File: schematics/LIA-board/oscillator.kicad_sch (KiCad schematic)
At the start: 7 parts, among them U6 OPA2196xD

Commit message: additions to pcb
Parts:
- added D2, D3: 1N4448W, Diode_SMD:D_SOD-123, symbol Diode:1N4448W
- added R14, R15, R16, R17, R18, R19, R20, R21, R22, R23: 1k, SparkFun-Resistor:R_0603_1608Metric, symbol SparkFun:R
- added U7: OPA2196xD, Package_SO:SOIC-8_3.9x4.9mm_P1.27mm, symbol Amplifier_Operational:OPA2196xD
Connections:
- net at C16.2, U6.7: now also R7.2, R9.1, R15.2, R18.1, R20.2; no longer R6.2
- net at C16.1, U6.6 (-): now also D2.2 (A), R17.1; no longer R9.1
- net at R9.2: now also R6.2, U6.2 (-), R14.2; no longer U6.3 (+)
- net GND: no longer names the net of C17.2
- net GND: now also R14.1, R21.2, U7.1
- new net: R17.2, R6.1, U6.1
- new net: D2.1 (K), R15.1, R16.2
- new net: R7.1, U6.3 (+)
- new net: C17.1, R20.1, U7.2 (-)
- new net: D3.1 (K), U6.5 (+), U7.3 (+)
- new net: R23.1, U7.5 (+)
- new net: R21.1, R22.2, U7.6 (-)
- new net: R22.1, U7.7
- new net: D3.2 (A), R18.2, R19.1
- now unconnected: C18.1, C18.2
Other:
- moved on the sheet: C16, C17, C18, R6, R7, R9, U6A, U6B, U6C

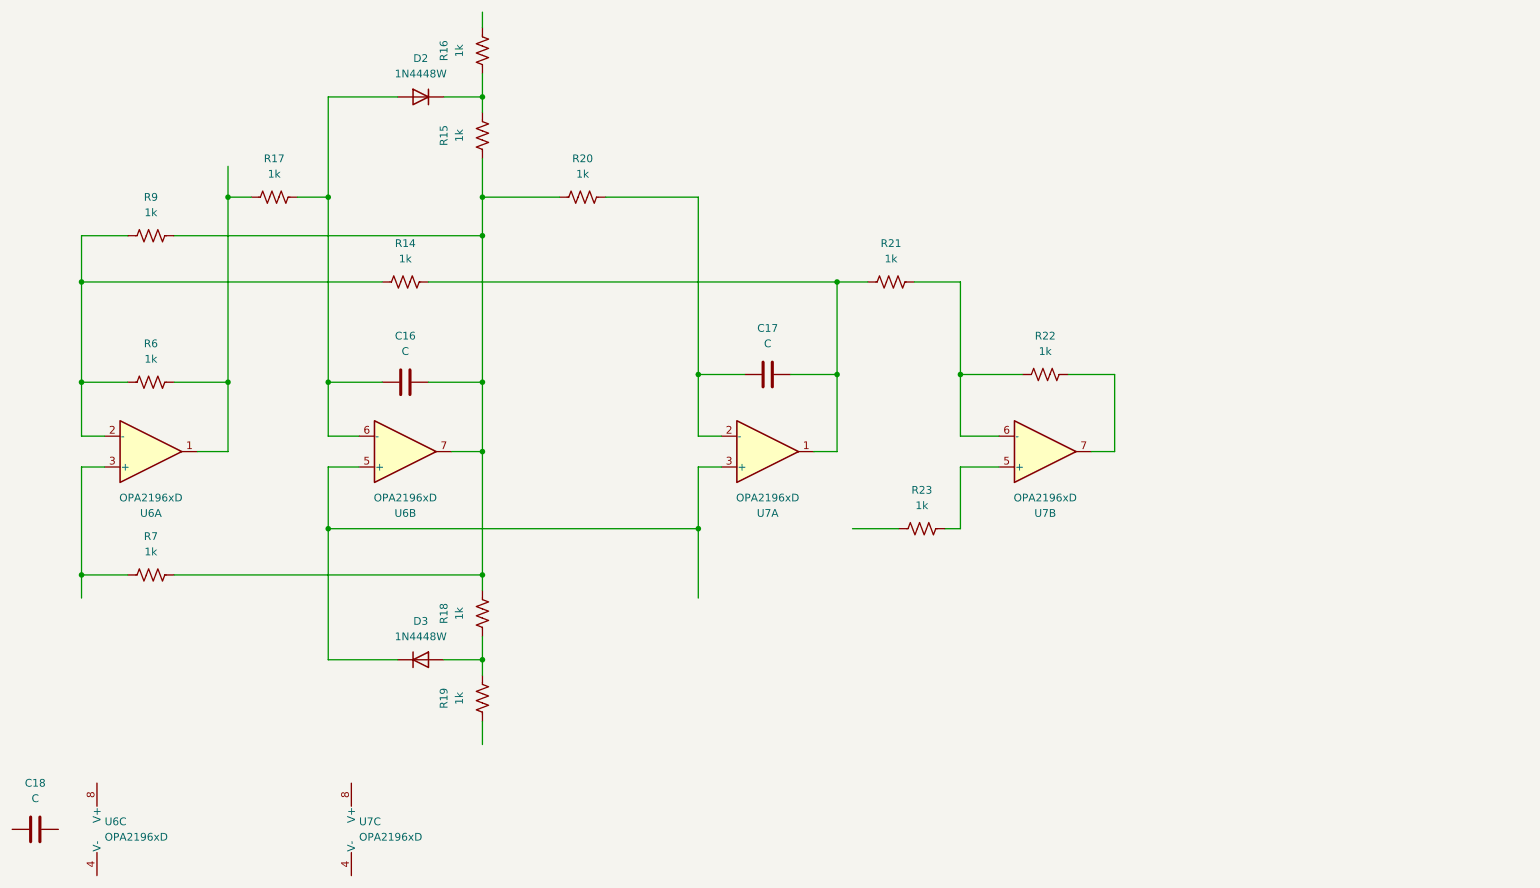
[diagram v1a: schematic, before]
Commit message: some simulations, new page in kicad scematic
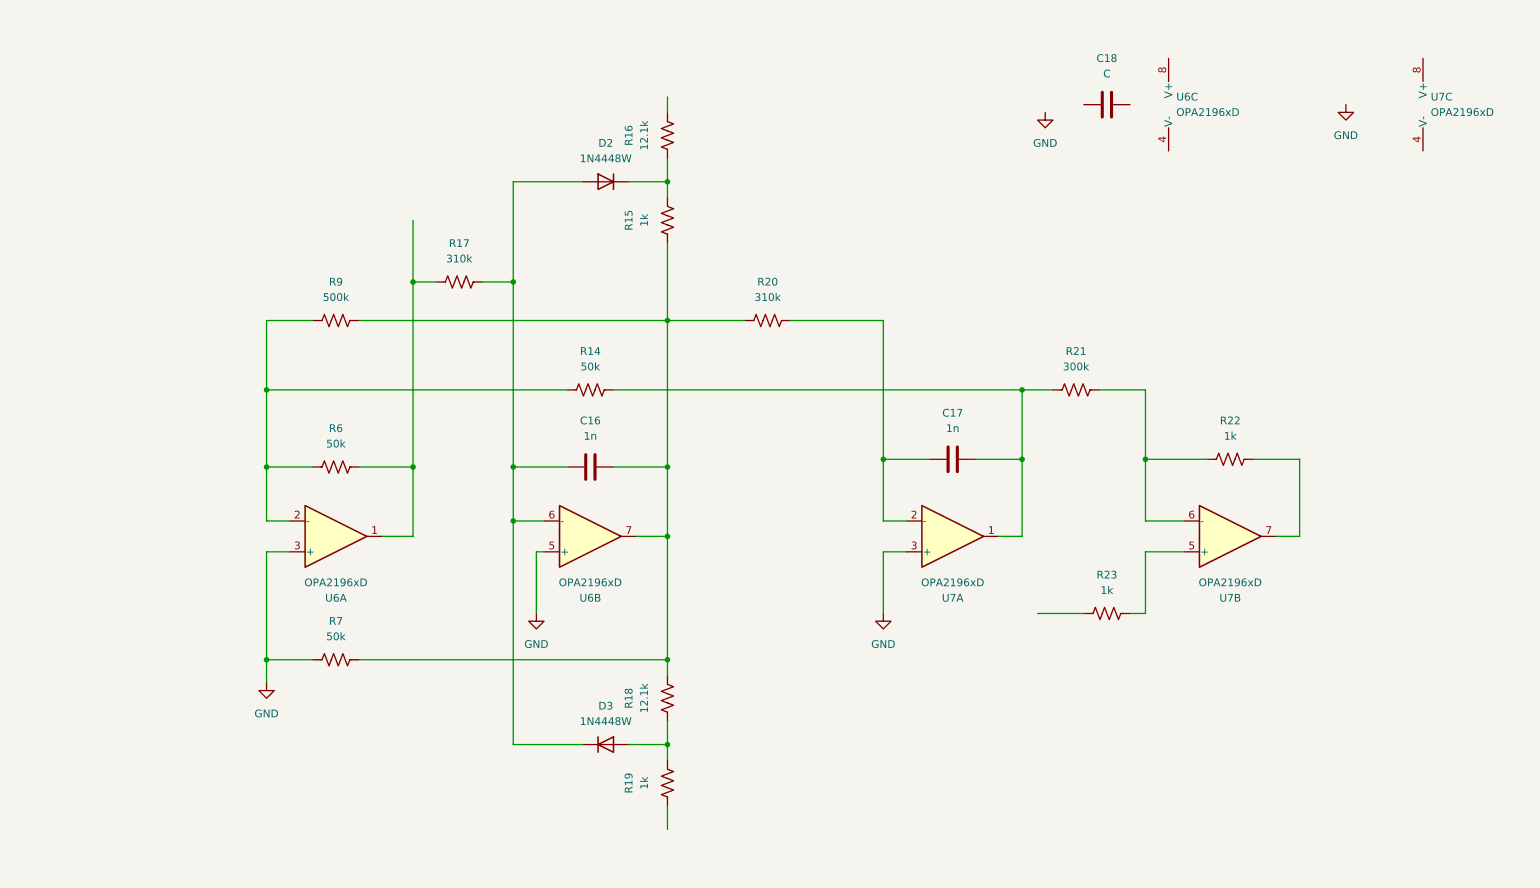
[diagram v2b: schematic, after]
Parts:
- C16, C17: value C -> 1n
- R14, R6, R7: value 1k -> 50k
- R16, R18: value 1k -> 12.1k
- R17, R20: value 1k -> 310k
- R21: value 1k -> 300k
- R9: value 1k -> 500k
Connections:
- net at C16.1, D2.2 (A), R17.1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: now also D3.1 (K)
- net GND: now reaches R7.1, U6.3 (+)
- net GND: now also U6.5 (+), U7.3 (+)
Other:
- moved on the sheet: C16, C17, C18, D2, D3, R14, R15, R16, R17, R18, R19, R20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

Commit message: all current changes
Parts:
- added C27, C28, C29: C, symbol Device:C
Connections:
- net GND: now also C18.1, C27.2, C28.1, C29.2
- net sin: now reaches R17.2, R6.1, U6.1
- net cos: now reaches C16.2, R15.2, R18.1, R20.2, R7.2, R9.1, U6.7
- net -5VA: now reaches U6.4 (V-)
- net -5VA: now also R19.2, U7.4 (V-), C27.1, C29.1
- net +5VA: now reaches U6.8 (V+)
- net +5VA: now also C18.2, R16.1, U7.8 (V+), C28.2
- net v_gate: now reaches R22.1, U7.7
- net gate_dc_bias: now reaches R23.2
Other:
- moved on the sheet: C18, U6C, U7C
